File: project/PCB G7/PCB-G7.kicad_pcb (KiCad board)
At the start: 2 copper layers, 23 parts, among them J13 Conn_01x03, J14 Conn_01x03, J2 Conn_01x02, J9 Micro_SD_Card, U1 ESP32-S3-UNO

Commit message: update schematics et pcb
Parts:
- removed A1, A2: Pololu_Breakout_A4988, Module:Pololu_Breakout-16_15.2x20.3mm
- removed C1, C2: 100uF, Capacitor_THT:C_Radial_D8.0mm_H7.0mm_P3.50mm
- removed F1: 3A, Fuse:Fuse_Littelfuse_395Series
- removed J13, J14, Jumper1, Jumper2, Servo-moteur1: Conn_01x03, Connector_PinHeader_2.54mm:PinHeader_1x03_P2.54mm_Vertical
- removed J9: Micro_SD_Card, Connector_Card:SD_Hirose_DM1AA_SF_PEJ82
- removed LCD1, STEPPER1, STEPPER2: Conn_01x04, Connector_PinHeader_2.54mm:PinHeader_1x04_P2.54mm_Vertical
- removed R1: 10k, Resistor_THT:R_Axial_DIN0207_L6.3mm_D2.5mm_P10.16mm_Horizontal
- removed R2, R3: 4.7k, Resistor_THT:R_Axial_DIN0207_L6.3mm_D2.5mm_P10.16mm_Horizontal
- removed U1: ESP32-S3-UNO, makerspace-unilasalle:ESP_S3_UNO
- removed bas1, haut1, retour1, selectionner1: SW_Push, Button_Switch_THT:SW_Tactile_Straight_KSA0Axx1LFTR
- added A5: driver A4988 1, Module:Pololu_Breakout-16_15.2x20.3mm, F.Cu at (37.8, 84.0)
- added A6: driver A4988 1, Module:Pololu_Breakout-16_15.2x20.3mm, F.Cu at (54.6, 84.0)
- added C7: 100uf, Capacitor_SMD:C_1206_3216Metric_Pad1.33x1.80mm_HandSolder, F.Cu at (197.9, 86.5)
- added C8: 100uf, Capacitor_SMD:C_1206_3216Metric_Pad1.33x1.80mm_HandSolder, F.Cu at (192.4, 86.5)
- added F3: 3A, Fuse:Fuseholder_Blade_Mini_Keystone_3568, F.Cu at (175.0, 78.3)
- added J18: Barrel_Jack_Switch, Connector_BarrelJack:BarrelJack_Horizontal, F.Cu at (168.0, 80.0)
- added J20: Oled, Display:OLED-128O064D, F.Cu at (245.3, 109.5)
- added R7: 10k, Resistor_THT:R_Axial_DIN0207_L6.3mm_D2.5mm_P10.16mm_Horizontal, F.Cu at (102.2, 74.8)
- added R8: 10k, Resistor_THT:R_Axial_DIN0207_L6.3mm_D2.5mm_P10.16mm_Horizontal, F.Cu at (102.2, 78.8)
- added U3: ESP32-S3-UNO, makerspace-unilasalle:ESP_S3_UNO, F.Cu at (72.6, 32.4)
- added U4: R-78E5.0-1.0, Converter_DCDC:Converter_DCDC_RECOM_R-78E-0.5_THT, F.Cu at (192.6, 82.2)
- J2: value Conn_01x02 -> Micro_SD_Card; footprint Connector_PinHeader_2.54mm:PinHeader_1x02_P2.54mm_Vertical -> Connector_Card:SD_Hirose_DM1AA_SF_PEJ82
- moved J2 33.5 mm to (99.6, 48.1)
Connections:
- J2 pad 1: GNDPWR -> unconnected-(J2-DAT2-Pad1)
- J2 pad 2: +12V -> CS

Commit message: update pcb
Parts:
- added C10: 100uf, makerspace-unilasalle:C_1206, F.Cu at (176.8, 84.4)
- added C11: 100uf, Capacitor_SMD:C_1206_3216Metric, F.Cu at (175.8, 94.3)
- added C12: 100uf, makerspace-unilasalle:C_1206, F.Cu at (140.5, 87.0)
- added C13: 100uf, makerspace-unilasalle:C_1206, F.Cu at (140.5, 89.5)
- added C5: 100uf, Capacitor_THT:C_Radial_D8.0mm_H11.5mm_P3.50mm, F.Cu at (158.0, 121.5)
- added C6: 100uf, Capacitor_THT:C_Radial_D8.0mm_H11.5mm_P3.50mm, F.Cu at (178.8, 121.9)
- added C9: 100uf, makerspace-unilasalle:C_1206, F.Cu at (181.2, 143.0)
- added J13: jumper 1 2, Connector_PinHeader_2.54mm:PinHeader_1x03_P2.54mm_Vertical, F.Cu at (178.3, 98.6)
- added J14: jumper 2 2, Connector_PinHeader_2.54mm:PinHeader_1x03_P2.54mm_Vertical, F.Cu at (156.5, 98.3)
- added J15: stepper 1, Connector_PinHeader_2.54mm:PinHeader_1x04_P2.54mm_Vertical, F.Cu at (164.5, 121.1)
- added J16: jumper 2 1, Connector_PinHeader_2.54mm:PinHeader_1x03_P2.54mm_Vertical, F.Cu at (156.5, 100.9)
- added J17: stepper 1, Connector_PinHeader_2.54mm:PinHeader_1x04_P2.54mm_Vertical, F.Cu at (143.9, 121.0)
- added J19: servomoteur, Connector_PinHeader_2.54mm:PinHeader_1x03_P2.54mm_Vertical, F.Cu at (179.4, 95.1)
- added J9: jumper 1 1, Connector_PinHeader_2.54mm:PinHeader_1x03_P2.54mm_Vertical, F.Cu at (178.3, 101.1)
- added R10: 4.7k, makerspace-unilasalle:R_1206, F.Cu at (175.8, 77.9)
- added R9: 4.7k, makerspace-unilasalle:R_1206, F.Cu at (175.8, 80.4)
- A6: value driver A4988 1 -> driver A4988 2
- J20: footprint Display:OLED-128O064D -> Connector_PinHeader_2.54mm:PinHeader_1x04_P2.54mm_Vertical
- R7, R8: footprint Resistor_THT:R_Axial_DIN0207_L6.3mm_D2.5mm_P10.16mm_Horizontal -> makerspace-unilasalle:R_1206
- moved A5 129.6 mm to (163.1, 117.3), turned to 90 degrees
- moved J2 114.9 mm to (162.0, 144.5), turned to -90 degrees
- moved R8 105.0 mm to (181.2, 148.0), turned to 180 degrees
- moved R7 99.8 mm to (181.2, 135.8), turned to 180 degrees
- moved A6 92.8 mm to (141.3, 117.2), turned to 90 degrees
- moved U3 83.7 mm to (136.1, 86.9), turned to 90 degrees
- moved J20 69.3 mm to (180.3, 85.4), turned to 180 degrees
- moved C7 34.6 mm to (164.0, 93.0), turned to -90 degrees
- moved C8 28.5 mm to (164.0, 87.5), turned to -90 degrees
- moved U4 25.6 mm to (167.5, 87.6), turned to -90 degrees
- moved F3 20.5 mm to (154.5, 78.3)
- moved J18 19.0 mm to (149.0, 79.2)
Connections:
- J20 pad 2: +5V -> +3.3V
- U3 pad 10: EN1 -> unconnected-(U3-GPIO1/ADC1_CH0-Pad10)
- U3 pad 13: CS -> EN2
- U3 pad 14: EN2 -> unconnected-(U3-GPIO4/ADC1_CH3-Pad14)
- U3 pad 22: unconnected-(U3-GPIO14/ADC2_CH3-Pad22) -> STEP1
- U3 pad 23: unconnected-(U3-GPIO21-Pad23) -> EN1
- U3 pad 24: unconnected-(U3-GPIO46-Pad24) -> CS
- U3 pad 9: STEP1 -> unconnected-(U3-GPIO2/ADC1_CH1-Pad9)
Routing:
- net +3.3V: track 0.00 -> 279.0 mm
- net +12V: track 0.00 -> 149.1 mm
- net MOSI: track 0.00 -> 88.2 mm
- net GND: track 0.00 -> 82.2 mm
- net CS: track 0.00 -> 61.8 mm
- net +5V: track 0.00 -> 52.7 mm
- net SCK: track 0.00 -> 30.7 mm
- net MISO: track 0.00 -> 29.5 mm
- net EN2: track 0.00 -> 29.4 mm
- net DIR1: track 0.00 -> 22.7 mm
- net STEP1: track 0.00 -> 19.8 mm
- net STEP2: track 0.00 -> 16.1 mm
- net DIR2: track 0.00 -> 12.5 mm
- net Net-(F3-Pad1): track 0.00 -> 9.33 mm
- net servo: track 0.00 -> 8.90 mm
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- added copper zone on B.Cu, net GND
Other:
- board outline added: 56.5 x 88 mm

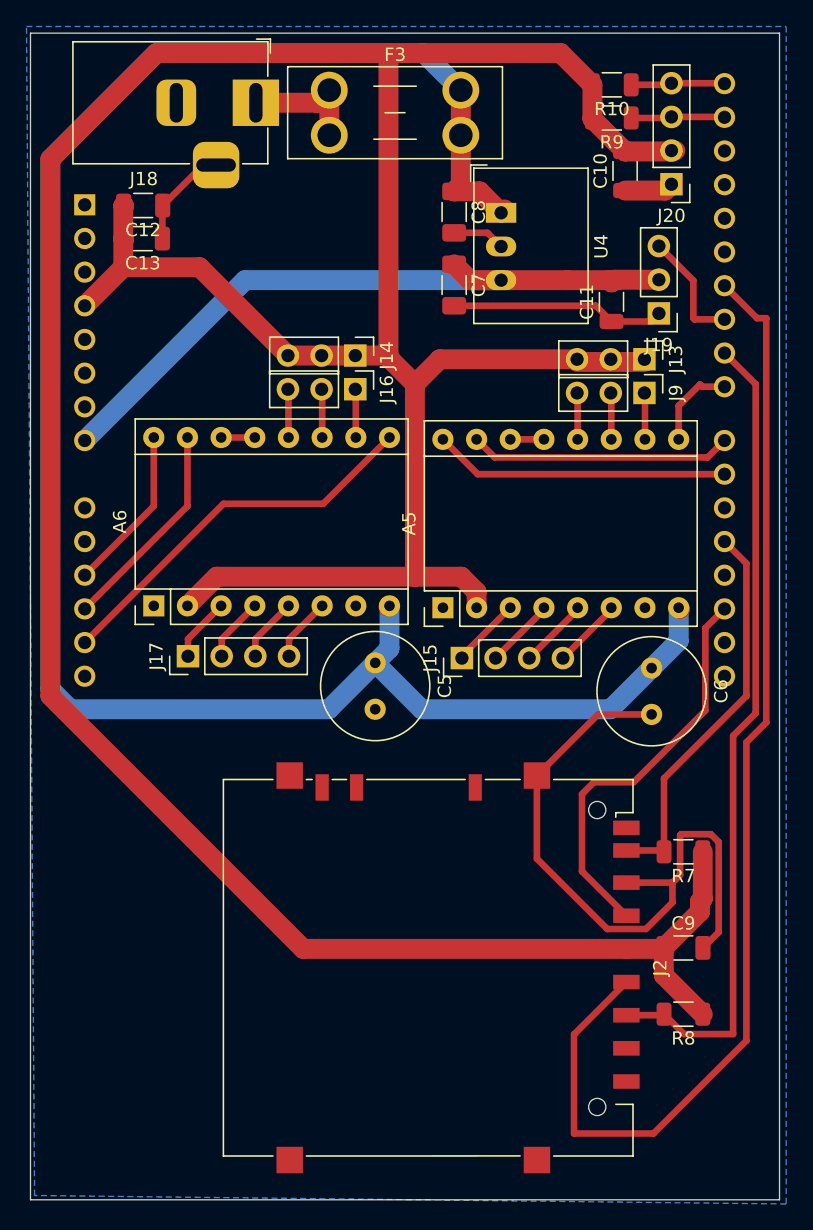
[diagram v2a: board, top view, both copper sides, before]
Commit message: Validation PCB pour production
Attention :
- Plan de masse sur les deux couches
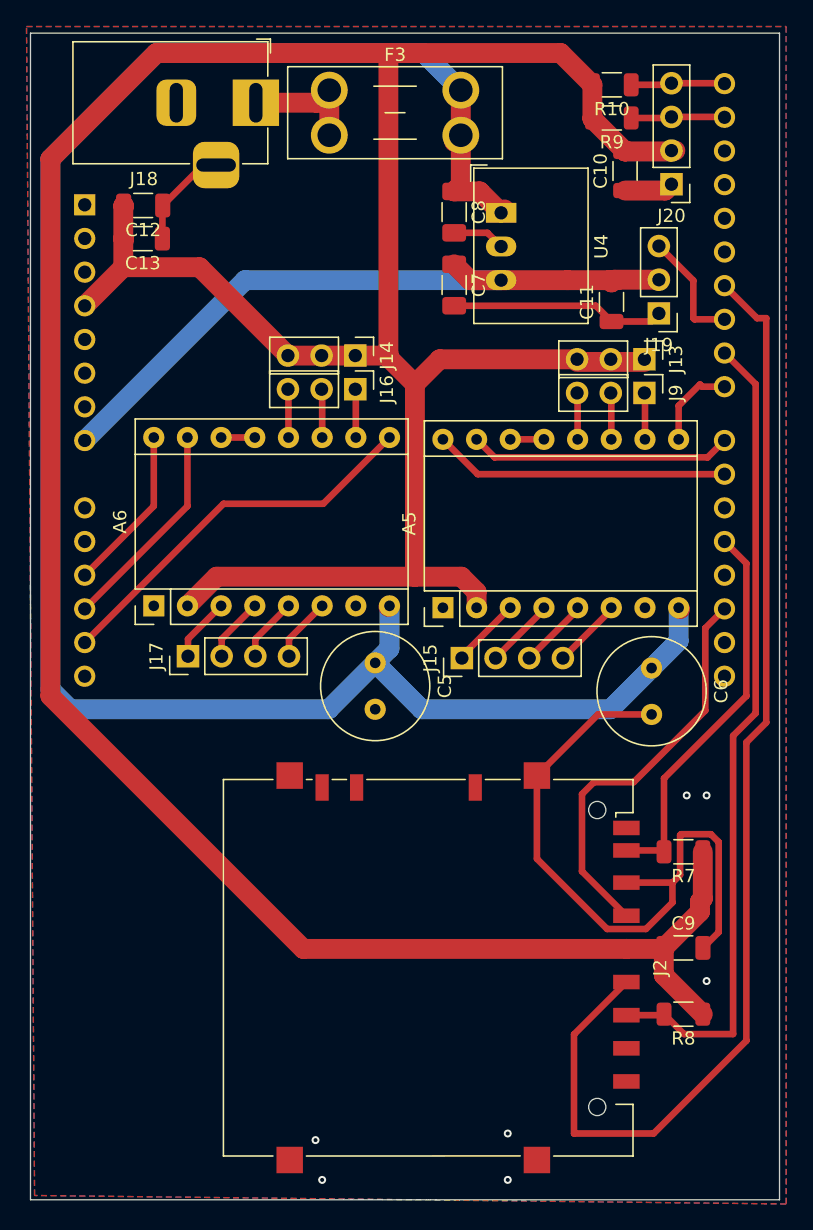
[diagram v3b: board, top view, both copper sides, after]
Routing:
- net GND: vias 0 -> 7
- added copper zone on F.Cu, net GND
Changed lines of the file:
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@@
+		(net "GND")
+	)
+	(via
+		(at 168 157)
+		(size 0.6)
+		(drill 0.3)
+		(layers "F.Cu" "B.Cu")
+		(free yes)
+		(net "GND")
+	)
+	(via
+		(at 154 160.5)
+		(size 0.6)
+		(drill 0.3)
+		(layers "F.Cu" "B.Cu")
+		(free yes)
+		(net "GND")
+	)
+	(via
+		(at 183 131.5)
+		(size 0.6)
+		(drill 0.3)
+		(layers "F.Cu" "B.Cu")
+		(free yes)
+		(net "GND")
+	)
+	(via
+		(at 181.5 131.5)
+		(size 0.6)
+		(drill 0.3)
+		(layers "F.Cu" "B.Cu")
+		(free yes)
+		(net "GND")
+	)
+	(via
+		(at 153.5 157.5)
+		(size 0.6)
+		(drill 0.3)
+		(layers "F.Cu" "B.Cu")
+		(free yes)
+		(net "GND")
+	)
+	(via
+		(at 168 160.5)
+		(size 0.6)
+		(drill 0.3)
+		(layers "F.Cu" "B.Cu")
+		(free yes)
+		(net "GND")
+	)
+	(via
+		(at 183 145.5)
+		(size 0.6)
+		(drill 0.3)
+		(layers "F.Cu" "B.Cu")
+		(free yes)
 		(net "GND")
 	)
@@
 	)
 	(segment
+		(start 180.35 80.3175)
+		(end 184.32 80.3175)
+		(width 0.5)
+		(layer "F.Cu")
+		(net "SDA")
+	)
+	(segment
+		(start 184.32 80.3175)
+		(end 184.35 80.3475)
+		(width 0.5)
+		(layer "F.Cu")
+		(net "SDA")
+	)
+	(segment
+		(start 177.3125 80.3975)
+		(end 180.27 80.3975)
+		(width 0.5)
+		(layer "F.Cu")
+		(net "SDA")
+	)
+	(segment
+		(start 180.27 80.3975)
+		(end 180.35 80.3175)
+		(width 0.5)
+		(layer "F.Cu")
+		(net "SDA")
+	)
+	(segment
+		(start 184.32 77.7775)
+		(end 184.35 77.8075)
+		(width 0.5)
+		(layer "F.Cu")
+		(net "SCL")
+	)
+	(segment
+		(start 180.23 77.8975)
+		(end 180.35 77.7775)
+		(width 0.5)
+		(layer "F.Cu")
+		(net "SCL")
+	)
+	(segment
+		(start 177.3125 77.8975)
+		(end 180.23 77.8975)
+		(width 0.5)
+		(layer "F.Cu")
+		(net "SCL")
+	)
+	(segment
+		(start 180.35 77.7775)
+		(end 184.32 77.7775)
+		(width 0.5)
+		(layer "F.Cu")
+		(net "SCL")
+	)
+	(segment
 		(start 167.5 92.6325)
 		(end 172.5 92.6325)
@@
 	)
 	(segment
-		(start 180.35 80.3175)
-		(end 184.32 80.3175)
-		(width 0.5)
-		(layer "F.Cu")
-		(net "SDA")
-	)
-	(segment
-		(start 184.32 80.3175)
-		(end 184.35 80.3475)
-		(width 0.5)
-		(layer "F.Cu")
-		(net "SDA")
-	)
-	(segment
-		(start 177.3125 80.3975)
-		(end 180.27 80.3975)
-		(width 0.5)
-		(layer "F.Cu")
-		(net "SDA")
-	)
-	(segment
-		(start 180.27 80.3975)
-		(end 180.35 80.3175)
-		(width 0.5)
-		(layer "F.Cu")
-		(net "SDA")
-	)
-	(segment
-		(start 184.32 77.7775)
-		(end 184.35 77.8075)
-		(width 0.5)
-		(layer "F.Cu")
-		(net "SCL")
-	)
-	(segment
-		(start 180.23 77.8975)
-		(end 180.35 77.7775)
-		(width 0.5)
-		(layer "F.Cu")
-		(net "SCL")
-	)
-	(segment
-		(start 177.3125 77.8975)
-		(end 180.23 77.8975)
-		(width 0.5)
-		(layer "F.Cu")
-		(net "SCL")
-	)
-	(segment
-		(start 180.35 77.7775)
-		(end 184.32 77.7775)
-		(width 0.5)
-		(layer "F.Cu")
-		(net "SCL")
-	)
-	(segment
 		(start 182.0875 95.5875)
 		(end 184.35 95.5875)
@@
 	(zone
 		(net "GND")
-		(layer "B.Cu")
+		(layers "F.Cu" "B.Cu")
 		(hatch edge 0.5)
 		(connect_pads

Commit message: fix some wiring problems
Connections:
- U3 pad 8: +5V -> +12V
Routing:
- net +5V: track 52.7 -> 16.2 mm
- net +12V: track 149.1 -> 151.7 mm
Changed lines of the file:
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@@
 			(unit
 				(name "A")
-				(pins "20" "19" "1" "3" "9" "10" "11" "12" "13" "14" "5" "2" "7" "6"
-					"29" "4" "8" "16" "15" "30" "32" "31" "28" "27" "26" "25" "24" "23"
-					"22" "21" "18" "17"
+				(pins "20" "19" "1" "3" "9" "10" "11" "12" "13" "14" "5" "2" "6" "29"
+					"7" "4" "8" "16" "15" "30" "32" "31" "28" "27" "26" "25" "24" "23" "22"
+					"21" "18" "17"
 				)
 			)
@@
 			(layers "*.Cu" "*.Mask")
 			(remove_unused_layers no)
-			(net "+5V")
+			(net "+12V")
 			(pinfunction "Vin_8")
 			(pintype "power_in")
@@
 	)
 	(segment
-		(start 136.09 104.7275)
-		(end 148.185 92.6325)
-		(width 1.5)
-		(layer "B.Cu")
-		(net "+5V")
-	)
-	(segment
-		(start 148.185 92.6325)
-		(end 167.5 92.6325)
-		(width 1.5)
-		(layer "B.Cu")
-		(net "+5V")
-	)
-	(segment
 		(start 182.0875 95.5875)
 		(end 184.35 95.5875)
@@
 	(segment
 		(start 133.5 123.5)
-		(end 133.5 83.5)
+		(end 133.5 104.75)
 		(width 1.5)
 		(layer "B.Cu")
@@
 	)
 	(segment
+		(start 133.5 104.75)
+		(end 133.5 83.5)
+		(width 1.5)
+		(layer "B.Cu")
+		(net "+12V")
+	)
+	(segment
 		(start 133.5 83.5)
 		(end 141.5 75.5)
@@
 	)
 	(segment
+		(start 133.5225 104.7275)
+		(end 136.09 104.7275)
+		(width 1.5)
+		(layer "B.Cu")
+		(net "+12V")
+	)
+	(segment
 		(start 154.5 125)
 		(end 135 125)
 		(width 1.5)
 		(layer "B.Cu")
+		(net "+12V")
+	)
+	(segment
+		(start 133.5 104.75)
+		(end 133.5225 104.7275)
+		(width 1.5)
+		(layer "B.Cu")
